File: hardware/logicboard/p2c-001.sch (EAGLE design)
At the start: 45 parts, among them IC1 74LS07N, K1 G5V1, T1 2SC1815

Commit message: Pinhead.
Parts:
- removed PWM: (no value), SparkFun-Connectors:CONN_08"
- removed PWR: (no value), SparkFun-Connectors:CONN_02
- added DIGITAL: (no value), SparkFun-Connectors:CONN_09
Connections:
- net GND: now also DIGITAL.2; no longer PWM.8, PWR.2
- net PWM_0: now also DIGITAL.3; no longer PWM.1
- net PWM_1: now also DIGITAL.4; no longer PWM.2
- net PWM_2: now also DIGITAL.5; no longer PWM.3
- net PWM_3: now also DIGITAL.6; no longer PWM.4
- net PWM_4: now also DIGITAL.7; no longer PWM.5
- net PWM_5: now also DIGITAL.8; no longer PWM.6
- net PWM_6: now also DIGITAL.9; no longer PWM.7
- net VIN: now also DIGITAL.1; no longer PWR.1

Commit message: Moved LEDs up.
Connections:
- net N$1 renamed RLYDRV
- net N$7 renamed RST
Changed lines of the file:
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@@
 </segment>
 </net>
-<net name="N$7" class="0">
+<net name="RST" class="0">
 <segment>
 <pinref part="U$2" gate="G$1" pin="R@1"/>
@@
 </segment>
 </net>
-<net name="N$1" class="0">
+<net name="RLYDRV" class="0">
 <segment>
 <pinref part="R4" gate="G$1" pin="2"/>

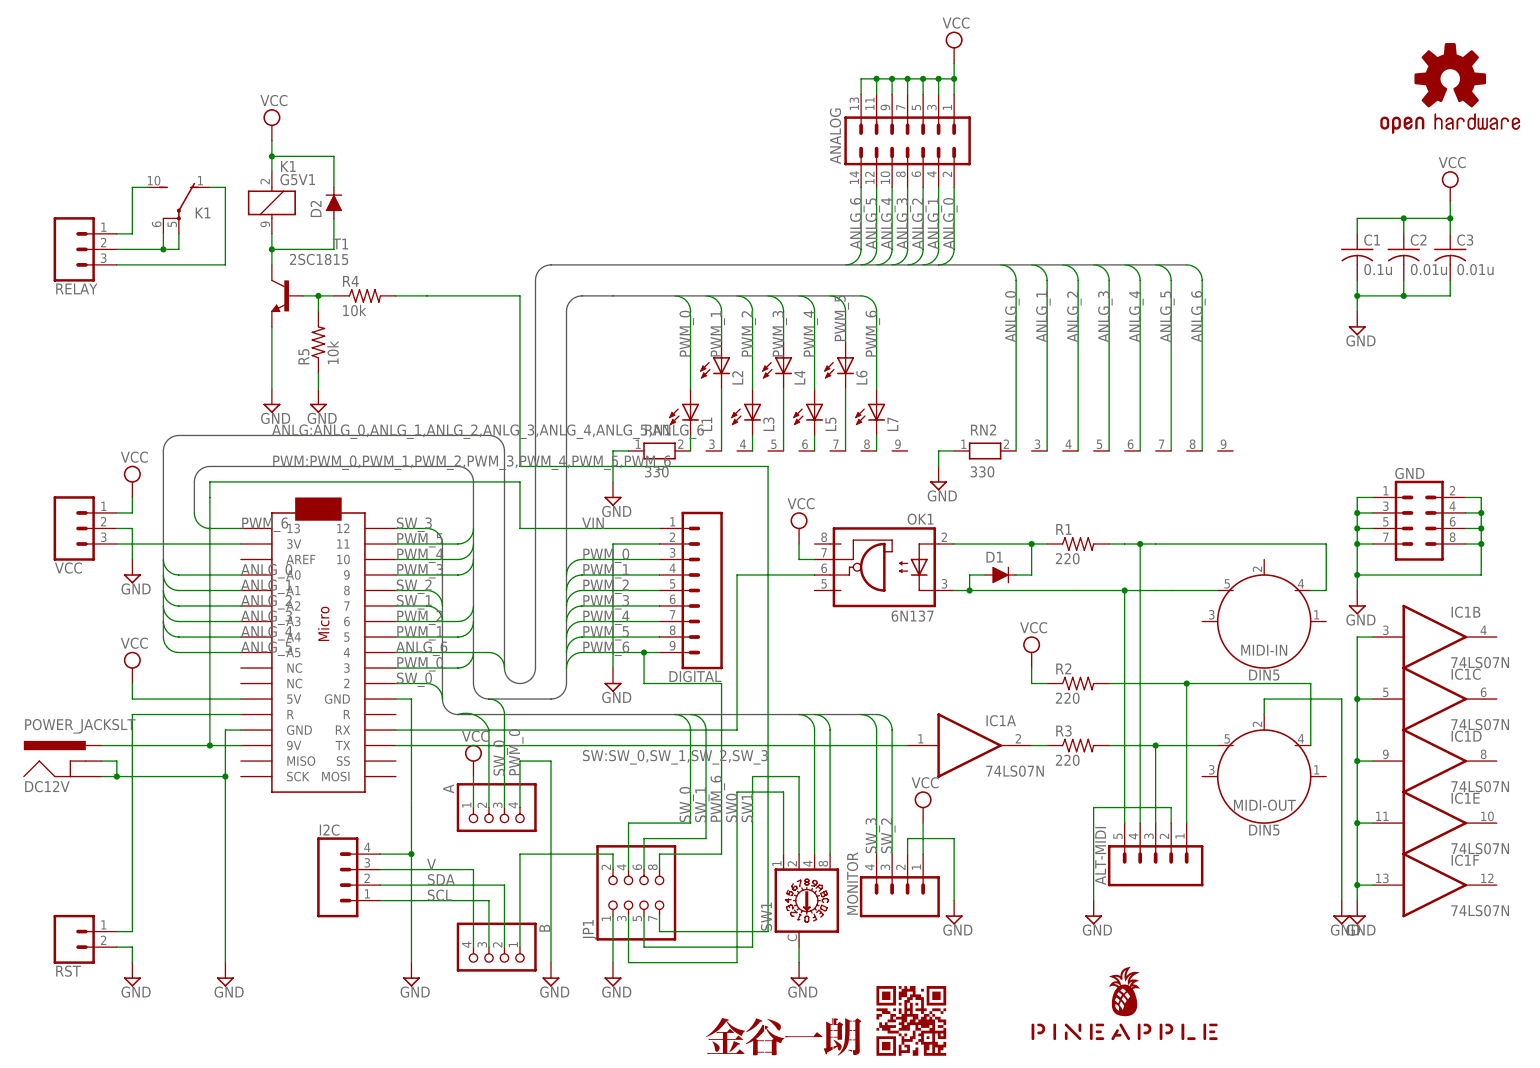
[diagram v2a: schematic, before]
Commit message: XOUT pins.
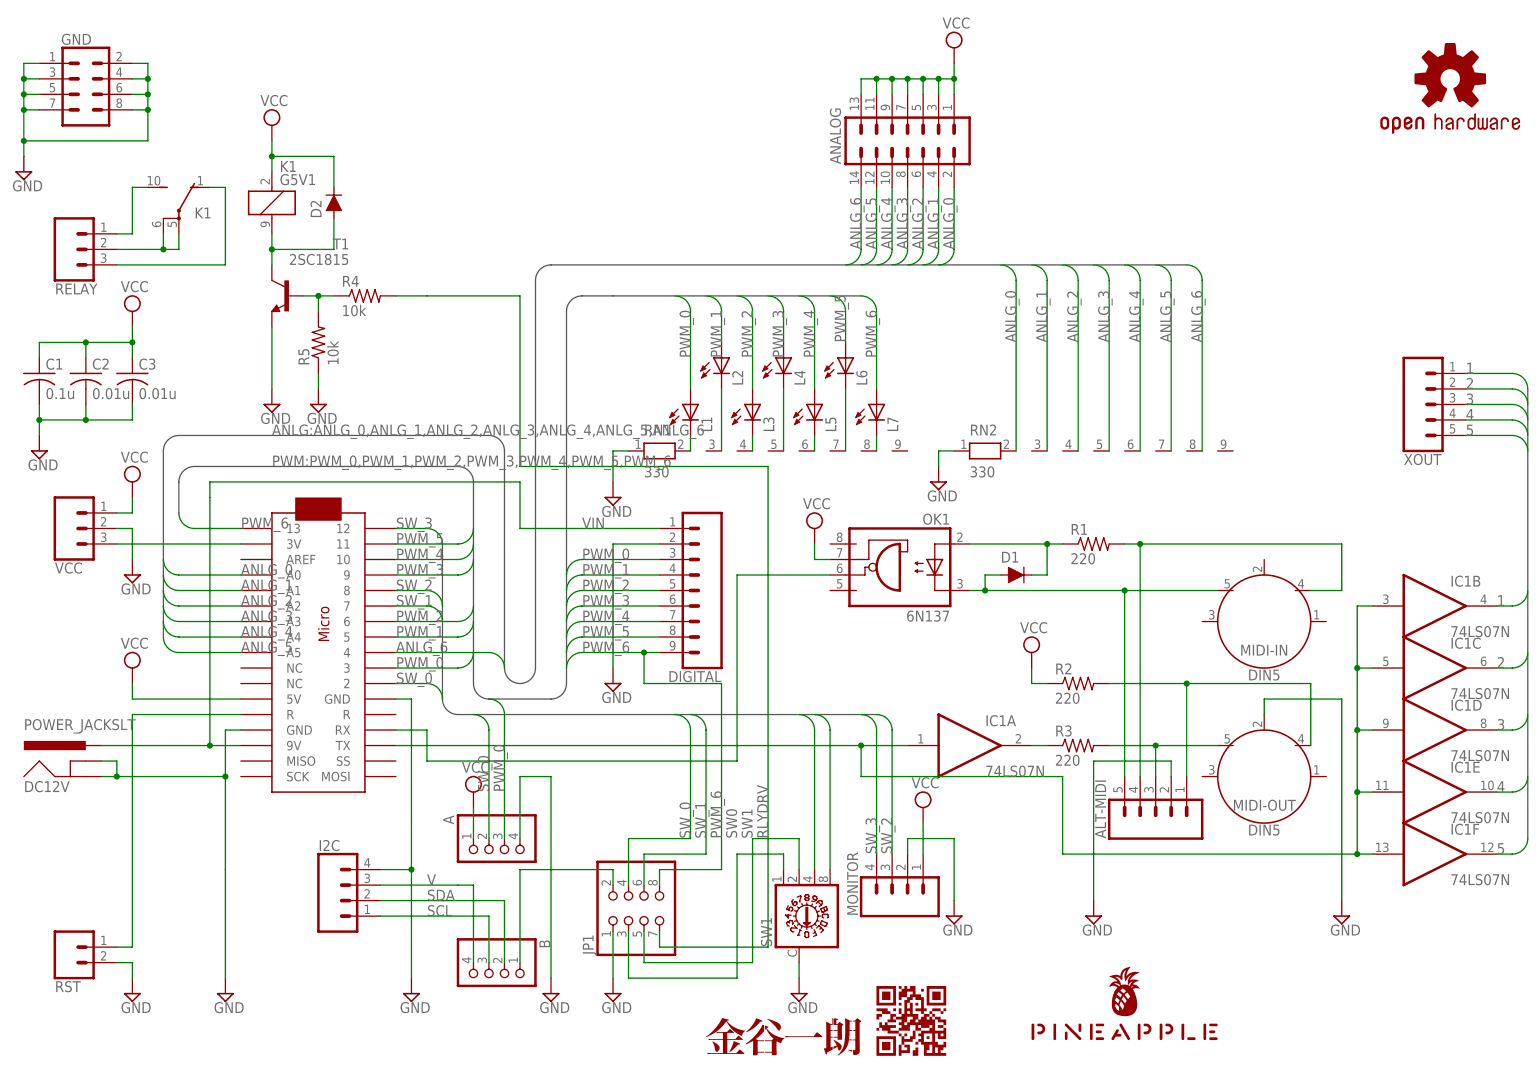
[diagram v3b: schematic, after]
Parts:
- added XOUT: (no value), SparkFun-Connectors:CONN_05
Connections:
- new net 1: IC1B.O, XOUT.1
- new net 2: IC1C.O, XOUT.2
- new net 3: IC1D.O, XOUT.3
- new net 4: IC1E.O, XOUT.4
- new net 5: IC1F.O, XOUT.5
- net GND: no longer IC1B.I, IC1C.I, IC1D.I, IC1E.I, IC1F.I
- net MIDIOUT: now also IC1B.I, IC1C.I, IC1D.I, IC1E.I, IC1F.I
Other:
- moved on the sheet: A, ALT-MIDI, B, C1, C2, C3, D1, GND, I2C, IC1B, IC1C, IC1D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

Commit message: New logo, new QR code.
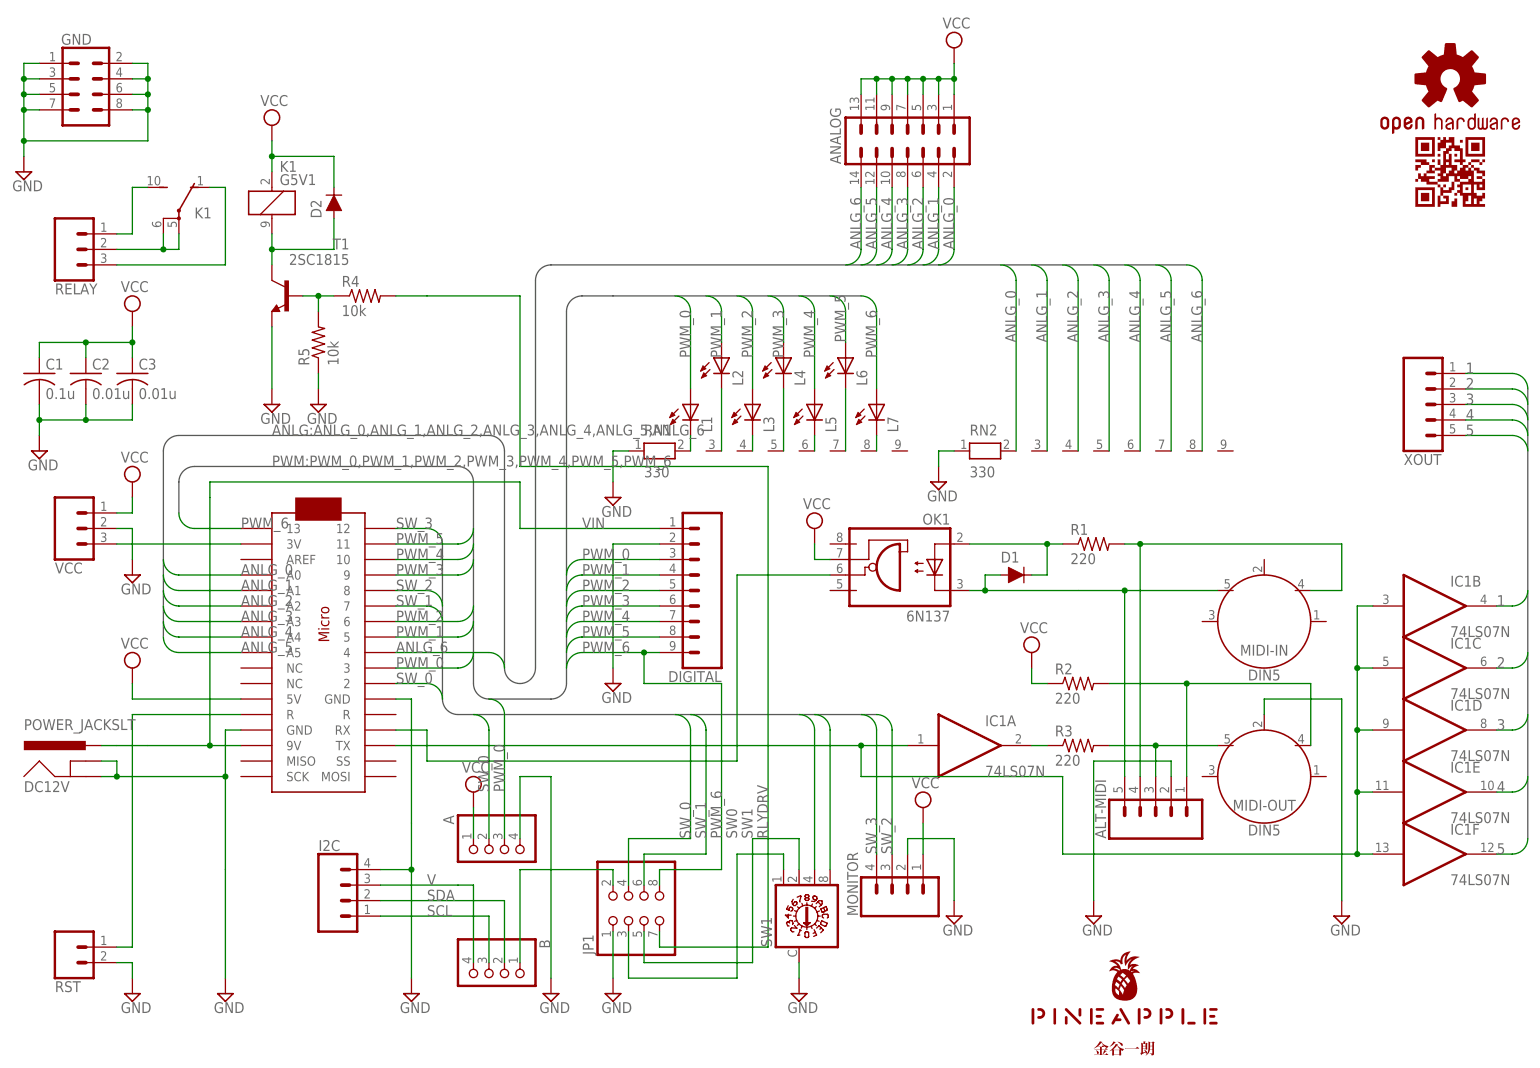
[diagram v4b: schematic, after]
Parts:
- U$3: value KANAYA_SILK -> KANAYA768_SILK; device kanaya:KANAYA_SILK -> pineapple:KANAYA768_SILK
- U$4: value PINEAPPLECARDQR_SILK -> CARDQRCODE450_SILK; device pineapplecardqr:PINEAPPLECARDQR_SILK -> pineapple:CARDQRCODE450_SILK
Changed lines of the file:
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@@
 <part name="SUPPLY19" library="supply2" library_urn="urn:adsk.eagle:library:372" deviceset="VCC" device=""/>
 <part name="SUPPLY20" library="supply2" library_urn="urn:adsk.eagle:library:372" deviceset="GND" device=""/>
-<part name="U$3" library="kanaya" deviceset="KANAYA_SILK" device=""/>
 <part name="R4" library="resistor" library_urn="urn:adsk.eagle:library:348" deviceset="R-US_" device="0204/5" package3d_urn="urn:adsk.eagle:package:25955/1" value="10k"/>
 <part name="T1" library="transistor" library_urn="urn:adsk.eagle:library:402" deviceset="2SC1815" device="" package3d_urn="urn:adsk.eagle:package:29929/2"/>
@@
 <part name="JP1" library="pinhead" library_urn="urn:adsk.eagle:library:325" deviceset="PINHD-2X4" device="" package3d_urn="urn:adsk.eagle:package:22461/2"/>
 <part name="I2C" library="SparkFun-Connectors" library_urn="urn:adsk.eagle:library:513" deviceset="CONN_04" device="JST-PTH-VERT" package3d_urn="urn:adsk.eagle:package:38102/1"/>
-<part name="U$4" library="pineapplecardqr" deviceset="PINEAPPLECARDQR_SILK" device=""/>
+<part name="U$4" library="pineapple" deviceset="CARDQRCODE450_SILK" device=""/>
 <part name="SUPPLY24" library="supply2" library_urn="urn:adsk.eagle:library:372" deviceset="GND" device=""/>
 <part name="ALT-MIDI" library="SparkFun-Connectors" library_urn="urn:adsk.eagle:library:513" deviceset="CONN_05" device="JST" package3d_urn="urn:adsk.eagle:package:38120/1"/>
@@
 <part name="DIGITAL" library="SparkFun-Connectors" library_urn="urn:adsk.eagle:library:513" deviceset="CONN_09" device="" package3d_urn="urn:adsk.eagle:package:38153/1"/>
 <part name="XOUT" library="SparkFun-Connectors" library_urn="urn:adsk.eagle:library:513" deviceset="CONN_05" device="" package3d_urn="urn:adsk.eagle:package:38104/1"/>
+<part name="U$3" library="pineapple" deviceset="KANAYA768_SILK" device=""/>
 </parts>
 <sheets>
@@
 <instances>
 <instance part="FRAME1" gate="G$1" x="0" y="0"/>
-<instance part="U$1" gate="G$1" x="187.96" y="7.62"/>
+<instance part="U$1" gate="G$1" x="187.96" y="10.16"/>
 <instance part="U$2" gate="G$1" x="55.88" y="71.12" rot="R270"/>
 <instance part="SUPPLY1" gate="GND" x="71.12" y="15.24"/>
@@
 <instance part="SUPPLY19" gate="G$1" x="81.28" y="48.26"/>
 <instance part="SUPPLY20" gate="GND" x="93.98" y="15.24"/>
-<instance part="U$3" gate="G$1" x="132.08" y="5.08"/>
 <instance part="R4" gate="G$1" x="63.5" y="129.54"/>
 <instance part="T1" gate="G$1" x="50.8" y="129.54" rot="MR0"/>
@@
 <instance part="JP1" gate="A" x="109.22" y="27.94" rot="R90"/>
 <instance part="I2C" gate="G$1" x="60.96" y="30.48"/>
-<instance part="U$4" gate="G$1" x="147.32" y="5.08"/>
+<instance part="U$4" gate="G$1" x="241.3" y="149.86"/>
 <instance part="SUPPLY24" gate="GND" x="182.88" y="27.94"/>
 <instance part="ALT-MIDI" gate="G$1" x="193.04" y="43.18" rot="R90"/>
@@
 <instance part="DIGITAL" gate="G$1" x="121.92" y="81.28" rot="R180"/>
 <instance part="XOUT" gate="G$1" x="236.22" y="111.76" rot="MR180"/>
+<instance part="U$3" gate="G$1" x="187.96" y="5.08"/>
 </instances>
 <busses>

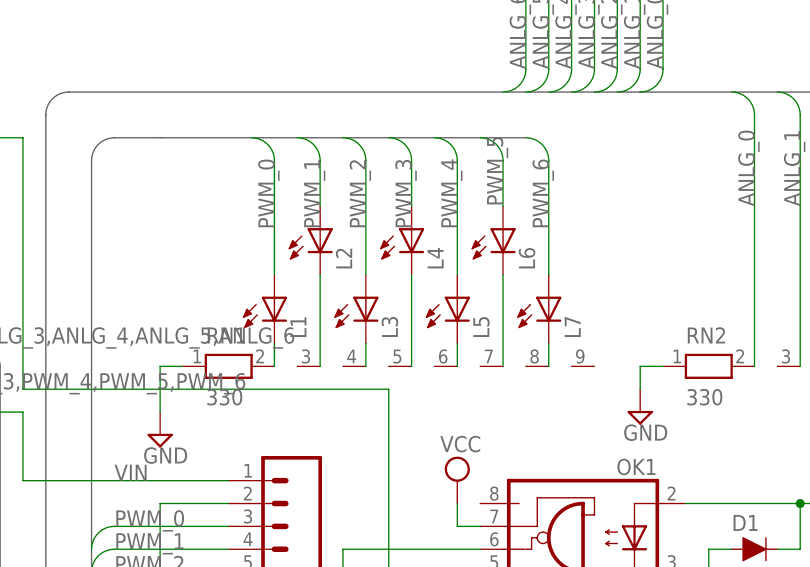
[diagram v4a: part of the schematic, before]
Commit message: Changed LED positions.
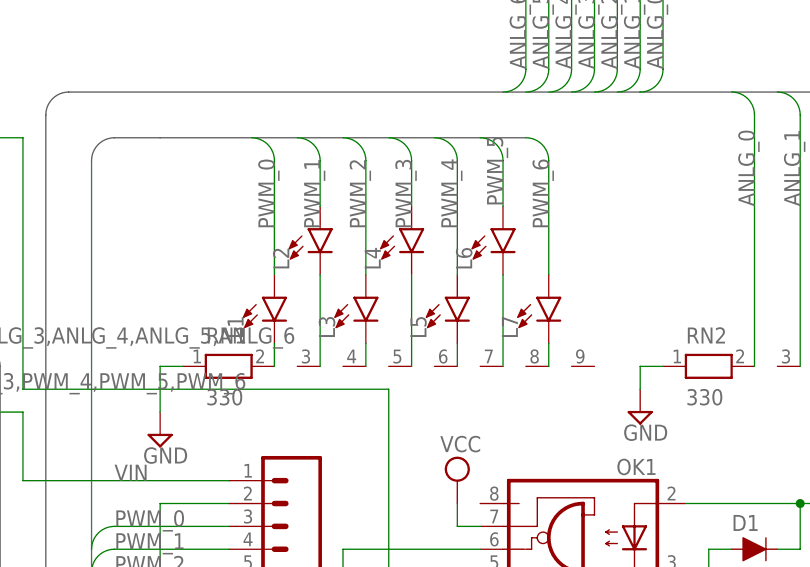
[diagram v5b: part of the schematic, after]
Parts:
- L1, L2, L3, L4, L5, L6, L7: device led:LEDB152 -> SparkFun-LED:LED-3MM-NO_SILK
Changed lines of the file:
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@@
 <part name="SW1" library="switch-dil" library_urn="urn:adsk.eagle:library:375" deviceset="A1353HEX" device="" package3d_urn="urn:adsk.eagle:package:27207/1"/>
 <part name="SUPPLY6" library="supply2" library_urn="urn:adsk.eagle:library:372" deviceset="GND" device=""/>
-<part name="L1" library="led" library_urn="urn:adsk.eagle:library:259" deviceset="LED" device="B152" package3d_urn="urn:adsk.eagle:package:15803/1"/>
-<part name="L2" library="led" library_urn="urn:adsk.eagle:library:259" deviceset="LED" device="B152" package3d_urn="urn:adsk.eagle:package:15803/1"/>
-<part name="L3" library="led" library_urn="urn:adsk.eagle:library:259" deviceset="LED" device="B152" package3d_urn="urn:adsk.eagle:package:15803/1"/>
-<part name="L4" library="led" library_urn="urn:adsk.eagle:library:259" deviceset="LED" device="B152" package3d_urn="urn:adsk.eagle:package:15803/1"/>
-<part name="L5" library="led" library_urn="urn:adsk.eagle:library:259" deviceset="LED" device="B152" package3d_urn="urn:adsk.eagle:package:15803/1"/>
-<part name="L6" library="led" library_urn="urn:adsk.eagle:library:259" deviceset="LED" device="B152" package3d_urn="urn:adsk.eagle:package:15803/1"/>
-<part name="L7" library="led" library_urn="urn:adsk.eagle:library:259" deviceset="LED" device="B152" package3d_urn="urn:adsk.eagle:package:15803/1"/>
+<part name="L1" library="SparkFun-LED" deviceset="LED" device="-3MM-NO_SILK"/>
+<part name="L2" library="SparkFun-LED" deviceset="LED" device="-3MM-NO_SILK"/>
+<part name="L3" library="SparkFun-LED" deviceset="LED" device="-3MM-NO_SILK"/>
+<part name="L4" library="SparkFun-LED" deviceset="LED" device="-3MM-NO_SILK"/>
+<part name="L5" library="SparkFun-LED" deviceset="LED" device="-3MM-NO_SILK"/>
+<part name="L6" library="SparkFun-LED" deviceset="LED" device="-3MM-NO_SILK"/>
+<part name="L7" library="SparkFun-LED" deviceset="LED" device="-3MM-NO_SILK"/>
 <part name="SUPPLY7" library="supply2" library_urn="urn:adsk.eagle:library:372" deviceset="GND" device=""/>
 <part name="RN1" library="resistor-net" library_urn="urn:adsk.eagle:library:343" deviceset="RN08" device="" package3d_urn="urn:adsk.eagle:package:24977/1" value="330"/>
